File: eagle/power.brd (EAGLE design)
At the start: 100 x 76.2 mm, 33 parts, among them IC1 LM317HV, IC2 LM317HV, IC3 LM317HV, IC4 7805TV, IC5 7805TV, IC6 7805TV, X1 22-23-2031, X10 22-23-2021, X11 22-23-2021, X2 22-23-2021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

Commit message: Correct missing connector on power board `
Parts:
- added X12: 22-23-2021, con-molex:22-23-2021
- moved X2 23.4 mm to (77.5, 12.7)
- moved X8 11.7 mm to (77.5, 21.6)
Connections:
- net GND: now also X12.2
- net N$3: now also X12.1
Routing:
- net N$3: track 170.8 -> 276.2 mm
- net N$9: track 222.6 -> 235.4 mm

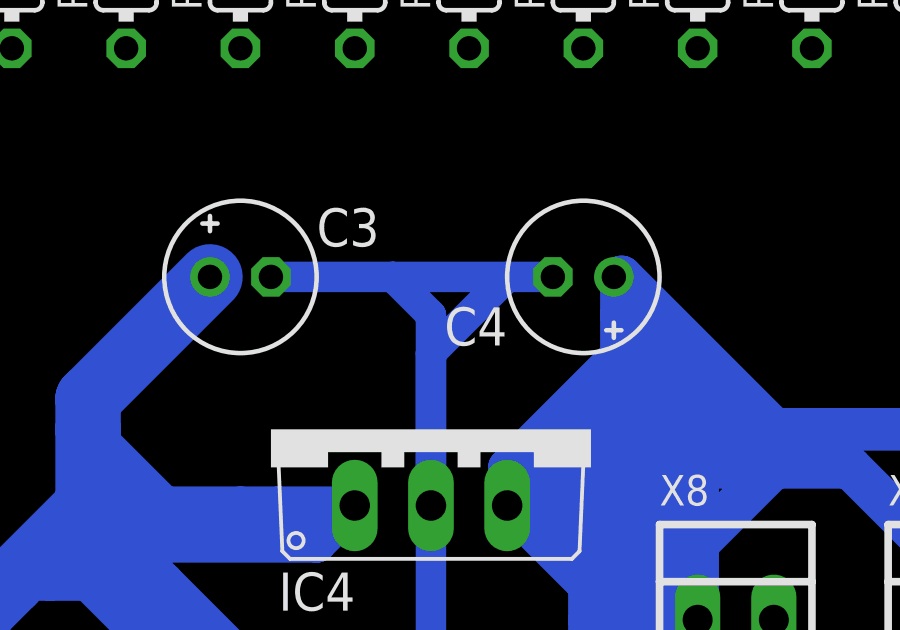
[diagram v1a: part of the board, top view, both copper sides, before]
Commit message: Fix up some polygon on power board
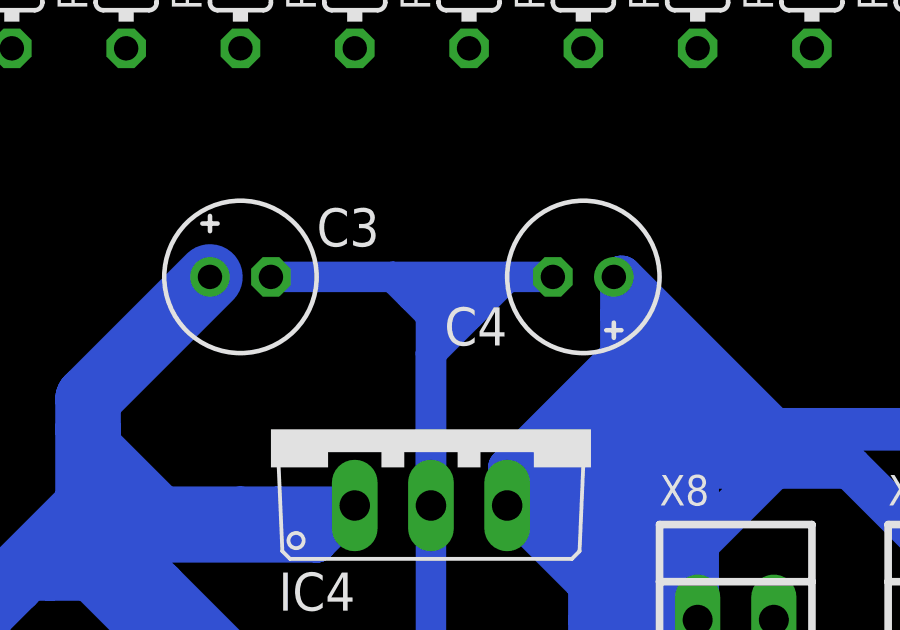
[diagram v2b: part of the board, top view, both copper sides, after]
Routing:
- net GND: track 46.0 -> 49.2 mm
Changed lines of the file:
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@@
 <wire x1="66.04" y1="33.02" x2="69.85" y2="33.02" width="1.016" layer="16"/>
 <wire x1="71.12" y1="33.02" x2="69.85" y2="33.02" width="1.016" layer="16"/>
-<wire x1="69.85" y1="33.02" x2="67.31" y2="30.48" width="1.016" layer="16"/>
+<wire x1="69.85" y1="33.02" x2="68.58" y2="31.75" width="1.016" layer="16"/>
+<wire x1="68.58" y1="31.75" x2="67.31" y2="30.48" width="1.016" layer="16"/>
 <wire x1="67.31" y1="30.48" x2="67.31" y2="25.4" width="1.016" layer="16"/>
 <wire x1="67.31" y1="25.4" x2="67.31" y2="31.75" width="1.016" layer="16"/>
-<wire x1="67.31" y1="31.75" x2="66.04" y2="33.02" width="1.016" layer="16"/>
+<wire x1="67.31" y1="31.75" x2="66.675" y2="32.385" width="1.016" layer="16"/>
+<wire x1="66.675" y1="32.385" x2="66.04" y2="33.02" width="1.016" layer="16"/>
 <wire x1="66.04" y1="33.02" x2="62.23" y2="33.02" width="1.016" layer="16"/>
 <contactref element="X12" pad="2"/>
+<wire x1="66.675" y1="32.385" x2="68.58" y2="32.385" width="0.8128" layer="16"/>
+<wire x1="68.58" y1="32.385" x2="68.58" y2="31.75" width="0.8128" layer="16"/>
+<wire x1="68.58" y1="31.75" x2="67.945" y2="31.75" width="0.8128" layer="16"/>
 <wire x1="62.23" y1="33.02" x2="61.976" y2="33.02" width="0" layer="19" extent="16-16"/>
 </signal>
@@
 <wire x1="55.88" y1="63.5" x2="55.88" y2="64.77" width="0.6096" layer="16"/>
 <wire x1="68.58" y1="63.5" x2="68.58" y2="67.31" width="0.6096" layer="16"/>
-<polygon width="0.6096" layer="16">
+<polygon width="0.6096" layer="16" thermals="no">
 <vertex x="43.18" y="67.31"/>
 <vertex x="40.64" y="64.77"/>
